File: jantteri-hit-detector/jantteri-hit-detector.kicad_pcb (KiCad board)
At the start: 2 copper layers, 88.9 x 19 mm, 35 parts, among them J1 SWD, J2 main_connector, J3 DBG_PORT, J4 LED_PORT, Q1 Si2319CDS, U1 STM32G030C8T6, U2 AMS1117-3.3, U3 KX023, U4 TXB0104RUT, U5 KX023, U6 KX023, Y1 16MHz

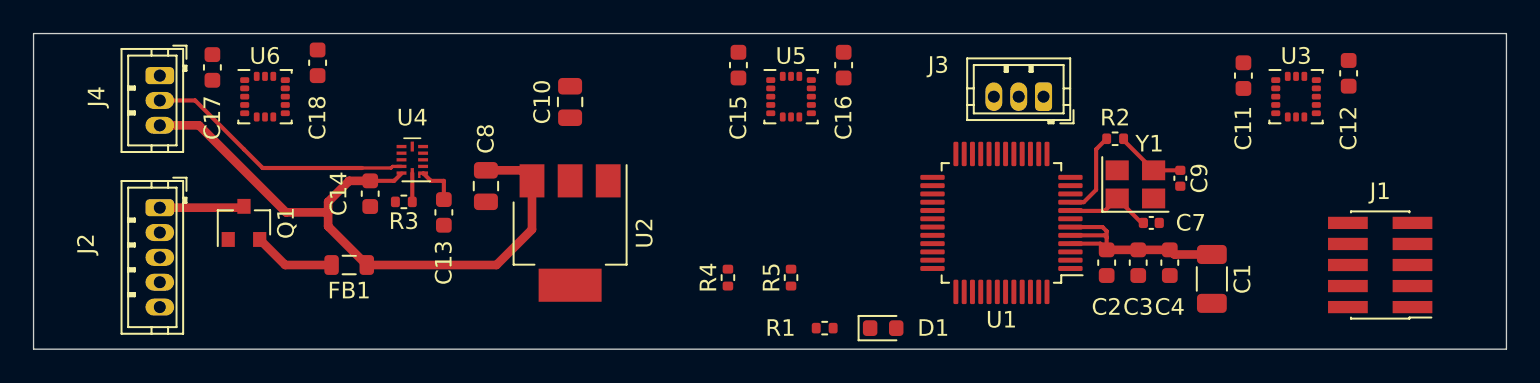
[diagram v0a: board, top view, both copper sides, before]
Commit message: remove hit-detector i2c pullup resistors
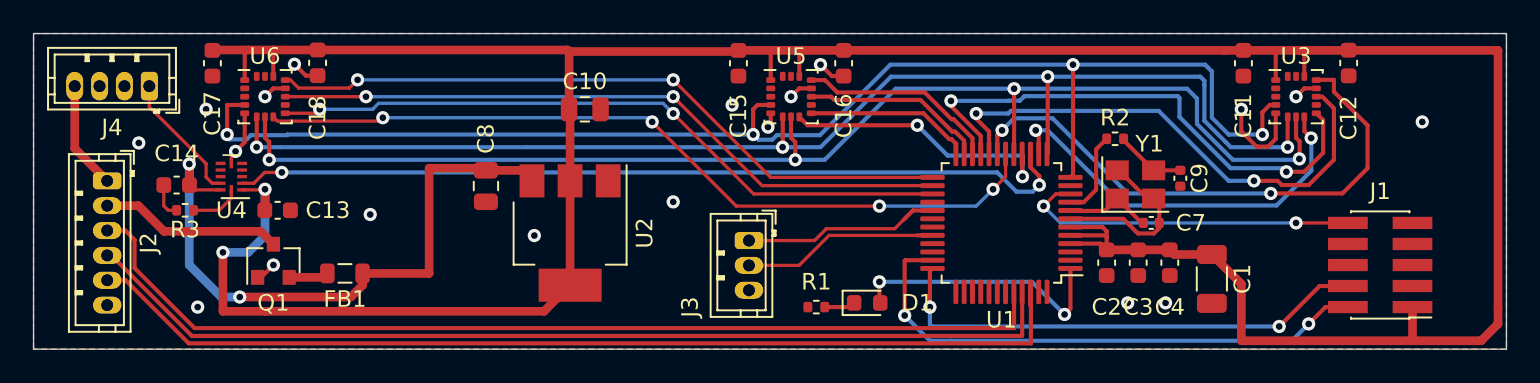
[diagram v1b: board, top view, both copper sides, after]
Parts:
- removed R4, R5: 4K7, Resistor_SMD:R_0402_1005Metric
- J2: value main_connector -> Conn_01x06_Male; footprint Connector_JST2:JST_ZH_B5B-ZR_1x05_P1.50mm_Vertical -> Connector_JST2:JST_ZH_B6B-ZR_1x06_P1.50mm_Vertical
- J4: value LED_PORT -> Conn_01x04_Male; footprint Connector_JST2:JST_ZH_B3B-ZR_1x03_P1.50mm_Vertical -> Connector_JST2:JST_ZH_B4B-ZR_1x04_P1.50mm_Vertical
- moved J3 19.8 mm to (143.5, 112.8), turned to 270 degrees
- moved R3 13.2 mm to (109.5, 111.0)
- moved C14 11.7 mm to (109.0, 109.5), turned to 180 degrees
- moved U4 11.0 mm to (112.3, 109.0)
- moved C13 10.0 mm to (115.1, 111.0), turned to 0 degrees
- moved J2 3.56 mm to (104.8, 109.2)
- moved Q1 2.90 mm to (114.8, 114.0)
- moved D1 1.80 mm to (150.6, 116.6)
- moved R1 1.37 mm to (147.6, 116.8)
- moved C10 0.99 mm to (133.6, 104.9), turned to 0 degrees
- moved J4 0.90 mm to (107.3, 103.5), turned to 180 degrees
- moved C11 0.75 mm to (173.4, 102.1)
- moved C12 0.62 mm to (179.7, 102.1)
- moved FB1 0.57 mm to (119.1, 114.8)
- moved C17 0.25 mm to (111.1, 102.1)
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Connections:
- J2 pad 1: VDC -> +12V
- J2 pad 2: HIT_INT -> VDC
- J2 pad 3: HIT_SCL -> HIT_INT
- J2 pad 4: HIT_SDA -> HIT_SCL
- J2 pad 5: GND -> HIT_SDA
- J4 pad 1: GND -> LED_DATA_5V
- J4 pad 2: LED_DATA_5V -> GND
- J4 pad 3: +5V -> GND
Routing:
- net +3V3: track 17.0 -> 190.8 mm, vias 0 -> 2
- net KX_SCLK: track 0.00 -> 82.9 mm, vias 0 -> 4
- net KX_MISO: track 0.00 -> 78.6 mm, vias 0 -> 4
- net KX_MOSI: track 0.00 -> 77.3 mm, vias 0 -> 4
- net HIT_SDA: track 0.00 -> 60.5 mm
- net HIT_INT: track 0.00 -> 60.4 mm
- net HIT_SCL: track 0.00 -> 59.9 mm
- net LED_DATA_3V3: track 0.00 -> 51.1 mm, vias 0 -> 2
- net KX3_CS: track 0.00 -> 48.7 mm, vias 0 -> 4
- net KX3_INT2: track 0.00 -> 41.9 mm, vias 0 -> 2
- net KX3_TRIG: track 0.00 -> 41.9 mm, vias 0 -> 2
- net KX3_INT1: track 0.00 -> 41.3 mm, vias 0 -> 2
- net KX1_TRIG: track 0.00 -> 33.7 mm, vias 0 -> 2
- net SWDIO: track 0.00 -> 33.2 mm, vias 0 -> 2
- net KX1_INT2: track 0.00 -> 32.1 mm, vias 0 -> 2
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- added copper zone on B.Cu, net GND
- added copper zone on F.Cu, net GND

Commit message: hit-detector update
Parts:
- added C19: 10u, Capacitor_SMD:C_0805_2012Metric, F.Cu at (108.8, 38.3)
- added C20: 100n, Capacitor_SMD:C_0603_1608Metric, F.Cu at (109.6, 50.0)
- added C21: 100n, Capacitor_SMD:C_0603_1608Metric, F.Cu at (101.5, 51.7)
- added C22: 100n, Capacitor_SMD:C_0603_1608Metric, F.Cu at (97.8, 34.4)
- added C23: 100n, Capacitor_SMD:C_0603_1608Metric, F.Cu at (93.3, 34.4)
- added C5: 100n, Capacitor_SMD:C_0603_1608Metric, F.Cu at (133.3, 30.2)
- added C6: 100n, Capacitor_SMD:C_0603_1608Metric, F.Cu at (135.1, 30.2)
- added Q2: IRLML6402TRPBF, Package_TO_SOT_SMD:SOT-23, F.Cu at (112.3, 49.9)
- added R4: 100K, Resistor_SMD:R_0402_1005Metric, F.Cu at (107.2, 48.6)
- added R5: 100K, Resistor_SMD:R_0402_1005Metric, F.Cu at (95.5, 35.1)
- added U7: AP2301, Package_SO:MSOP-8-1EP_3x3mm_P0.65mm_EP1.68x1.88mm, F.Cu at (105.5, 50.9)
- added U8: TXB0104RUT, Package_DFN_QFN:Texas_R_PUQFN-N12, F.Cu at (95.6, 32.0)
- C10: value 10u -> 100n; footprint Capacitor_SMD:C_0805_2012Metric -> Capacitor_SMD:C_0603_1608Metric
- C18: value 100n -> 10u; footprint Capacitor_SMD:C_0603_1608Metric -> Capacitor_SMD:C_0805_2012Metric
- C7: value 12p -> 100n; footprint Capacitor_SMD:C_0402_1005Metric -> Capacitor_SMD:C_0603_1608Metric
- C8: value 10u -> 12p; footprint Capacitor_SMD:C_0805_2012Metric -> Capacitor_SMD:C_0402_1005Metric
- J1: value SWD -> Conn_01x06_Male; footprint Connector_PinHeader_1.27mm:PinHeader_2x05_P1.27mm_Vertical_SMD -> Connector_JST2:JST_ZH_B6B-ZR_1x06_P1.50mm_Vertical; moved to B.Cu
- J2: value Conn_01x06_Male -> SWD; footprint Connector_JST2:JST_ZH_B6B-ZR_1x06_P1.50mm_Vertical -> Connector_PinHeader_1.27mm:PinHeader_2x05_P1.27mm_Horizontal
- J3: value DBG_PORT -> DBG; footprint Connector_JST2:JST_ZH_B3B-ZR_1x03_P1.50mm_Vertical -> Connector_JST2:JST_ZH_B4B-ZR_1x04_P1.50mm_Vertical
- Q1: value Si2319CDS -> IRLML6402TRPBF
- R1: value 1k5 -> 47
- R2: value 47 -> 1k5
- U2: value AMS1117-3.3 -> AP2301; footprint Package_TO_SOT_SMD:SOT-223-3_TabPin2 -> Package_SO:MSOP-8-1EP_3x3mm_P0.65mm_EP1.68x1.88mm
- U4: value TXB0104RUT -> KX023; footprint Package_DFN_QFN:Texas_R_PUQFN-N12 -> Package_LGA:LGA-16_3x3mm_P0.5mm_LayoutBorder3x5y
- U6: value KX023 -> AMS1117-3.3; footprint Package_LGA:LGA-16_3x3mm_P0.5mm_LayoutBorder3x5y -> Package_TO_SOT_SMD:SOT-223-3_TabPin2
- moved J1 143.7 mm to (62.5, 33.9), turned to 270 degrees
- moved C12 120.7 mm to (85.0, 27.3), turned to 90 degrees
- moved U3 117.8 mm to (83.9, 31.2)
- moved C9 93.0 mm to (122.2, 29.1), turned to 90 degrees
- moved C4 91.9 mm to (131.6, 30.2), turned to 90 degrees
- moved C3 91.8 mm to (129.8, 30.2), turned to 90 degrees
- moved C2 91.7 mm to (128.1, 30.2), turned to 90 degrees
- moved C1 90.8 mm to (139.1, 30.4), turned to 90 degrees
- moved Y1 90.6 mm to (125.0, 29.1), turned to 180 degrees
- moved C11 90.0 mm to (99.6, 50.5)
- moved C13 89.6 mm to (83.1, 27.3), turned to 90 degrees
- moved R1 88.5 mm to (123.7, 31.6), turned to 180 degrees
- moved C7 87.2 mm to (136.9, 30.2), turned to 90 degrees
- moved D1 85.5 mm to (133.1, 32.9), turned to 180 degrees
- moved C8 82.8 mm to (125.1, 26.8), turned to 180 degrees
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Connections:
- net DBG_RX renamed /jst-dbg/DBG_RX
- net DBG_TX renamed /jst-dbg/DBG_TX
- net STATUS_LED renamed Net-(D1-Pad2)
- C10 pad 1: +3V3 -> Net-(C10-Pad1)
- C11 pad 1: +3V3 -> /power_protect/OUT
- C14 pad 1: +5V -> +3V3
- C18 pad 1: +3V3 -> +5V
- C7 pad 1: HSE_IN -> +3V3
- C8 pad 1: +5V -> /STM32G030C8T6/HSE_IN
- FB1 pad 2: Net-(FB1-Pad2) -> /power_protect/OUT
- J1 pad 1: +3V3 -> +12V
- J1 pad 2: SWDIO -> VCC
- J1 pad 3: GND -> HIT_INT
- J1 pad 4: SWCLK -> HIT_SCL
- J1 pad 5: GND -> HIT_SDA
- J1 pad 6: (no net) -> GND
- J2 pad 1: +12V -> +3V3
- J2 pad 2: VDC -> /10pinARM/SWDIO
- J2 pad 3: HIT_INT -> GND
- J2 pad 4: HIT_SCL -> /10pinARM/SWCLK
- J2 pad 5: HIT_SDA -> GND
- J2 pad 6: GND -> /10pinARM/SWO
- J3 pad 3: GND -> USB-5V
- J4 pad 1: LED_DATA_5V -> Net-(J4-Pad1)
- Q1 pad 2: Net-(FB1-Pad2) -> Net-(C10-Pad1)
- Q1 pad 3: VDC -> VCC
- R1 pad 1: GND -> /STM32G030C8T6/HSE_OUT
- R1 pad 2: Net-(D1-Pad1) -> Net-(C9-Pad1)
- R2 pad 1: HSE_OUT -> GND
- R2 pad 2: Net-(C9-Pad1) -> Net-(D1-Pad1)
- R3 pad 1: Net-(R3-Pad1) -> /power_protect/EN
- U1 pad 10: NRST -> /10pinARM/NRST
- U1 pad 11: (no net) -> /STM32G030C8T6/PA0
- U1 pad 14: KX1_CS -> /STM32G030C8T6/PA3
- U1 pad 16: KX2_CS -> /STM32G030C8T6/PA5
- U1 pad 18: KX3_CS -> /STM32G030C8T6/PA7
- U1 pad 19: KX1_TRIG -> KX1_INT1
- U1 pad 2: (no net) -> Net-(U1-Pad2)
- U1 pad 20: KX1_INT1 -> KX1_INT2
- U1 pad 21: KX1_INT2 -> KX2_TRIG
- U1 pad 22: KX2_TRIG -> KX1_CS
- U1 pad 23: KX2_INT1 -> KX2_INT2
- U1 pad 24: KX2_INT2 -> KX2_CS
- U1 pad 26: KX3_INT1 -> KX3_CS
- U1 pad 27: KX3_INT2 -> /STM32G030C8T6/PB15
- U1 pad 28: (no net) -> /STM32G030C8T6/PA8
- U1 pad 3: (no net) -> Net-(U1-Pad3)
- U1 pad 30: (no net) -> /STM32G030C8T6/PC6
- U1 pad 31: (no net) -> /STM32G030C8T6/PC7
- U1 pad 33: (no net) -> /STM32G030C8T6/PA11
- U1 pad 34: (no net) -> /STM32G030C8T6/PA12
- U1 pad 35: SWDIO -> /10pinARM/SWDIO
- U1 pad 36: SWCLK -> /10pinARM/SWCLK
- U1 pad 37: (no net) -> /STM32G030C8T6/PA15
- U1 pad 38: (no net) -> /STM32G030C8T6/PD0
- U1 pad 39: (no net) -> /STM32G030C8T6/PD1
- U1 pad 40: (no net) -> /STM32G030C8T6/PD2
- U1 pad 41: (no net) -> /STM32G030C8T6/PD3
- U1 pad 42: (no net) -> KX2_INT1
- U1 pad 43: (no net) -> KX3_INT1
- U1 pad 44: HIT_INT -> KX3_INT2
- U1 pad 47: (no net) -> HIT_INT
- U1 pad 48: (no net) -> KX1_TRIG
- U1 pad 8: HSE_IN -> /STM32G030C8T6/HSE_IN
- U1 pad 9: HSE_OUT -> /STM32G030C8T6/HSE_OUT
- U2 pad 2: +3V3 -> Net-(C10-Pad1)
- U2 pad 3: +5V -> Net-(C10-Pad1)
- U4 pad 10: LED_DATA_5V -> (no net)
- U4 pad 11: +5V -> KX2_INT1
- U4 pad 12: Net-(R3-Pad1) -> GND
- U4 pad 2: LED_DATA_3V3 -> (no net)
- U4 pad 4: (no net) -> KX_SCLK
- U4 pad 5: (no net) -> GND
- U4 pad 6: GND -> KX_MOSI
- U4 pad 7: (no net) -> KX_MISO
- U4 pad 8: (no net) -> KX2_CS
- U4 pad 9: (no net) -> KX2_INT2
- U5 pad 11: KX2_INT1 -> KX3_INT1
- U5 pad 13: KX2_TRIG -> KX3_TRIG
- U5 pad 8: KX2_CS -> KX3_CS
- U5 pad 9: KX2_INT2 -> KX3_INT2
- U6 pad 1: +3V3 -> GND
- U6 pad 2: (no net) -> +3V3
- U6 pad 3: (no net) -> +5V
- Y1 pad 1: HSE_IN -> /STM32G030C8T6/HSE_IN
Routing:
- net VCC: track 0.00 -> 57.6 mm, vias 0 -> 2
- net +3V3: track 190.8 -> 144.2 mm
- net SWDIO: track 33.2 -> 0.00 mm, vias 2 -> 0
- net SWCLK: track 29.7 -> 0.00 mm, vias 2 -> 0
- net /10pinARM/NRST: track 0.00 -> 24.9 mm, vias 0 -> 2
- net /10pinARM/SWDIO: track 0.00 -> 21.8 mm
- net KX3_INT2: track 41.9 -> 20.5 mm
- net NRST: track 20.7 -> 0.00 mm, vias 2 -> 0
- net KX1_CS: track 24.3 -> 43.7 mm
- net /10pinARM/SWCLK: track 0.00 -> 19.3 mm
- net KX2_INT1: track 11.1 -> 30.2 mm, vias 0 -> 2
- net LED_DATA_3V3: track 51.1 -> 32.2 mm, vias 2 -> 4
- net USB-5V: track 0.00 -> 18.1 mm
- net Net-(J4-Pad1): track 0.00 -> 17.9 mm
- net KX3_INT1: track 41.3 -> 23.5 mm
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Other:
- board size 88.9 x 19 mm -> 103.9 x 29.1 mm

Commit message: jantteri-pwr-motor
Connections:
- J3 pad 4: /jst-dbg/GND -> GND

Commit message: random changes
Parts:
- U3, U4, U5: value KX023 -> LIS2DW12TR; footprint Package_LGA:LGA-16_3x3mm_P0.5mm_LayoutBorder3x5y -> Package_LGA:LGA-12_2x2mm_P0.5mm
- moved C13 7.78 mm to (90.3, 30.1), turned to 270 degrees
- moved C14 6.73 mm to (106.9, 30.1), turned to 270 degrees
- moved C15 6.05 mm to (109.7, 30.1), turned to 270 degrees
- moved C12 3.63 mm to (87.2, 30.1), turned to 270 degrees
- moved C16 2.81 mm to (145.7, 28.7), turned to 0 degrees
- moved C17 0.86 mm to (145.7, 27.1), turned to 0 degrees
- moved U3 0.18 mm to (83.8, 31.1), turned to 90 degrees
- moved U4 0.14 mm to (114.0, 31.1), turned to 90 degrees
- moved U5 0.13 mm to (144.1, 31.1), turned to 90 degrees
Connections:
- U1 pad 21: KX2_TRIG -> KX2_INT1
- U1 pad 25: KX3_TRIG -> /STM32G030C8T6/PB13
- U1 pad 42: KX2_INT1 -> /STM32G030C8T6/PB3
- U1 pad 48: KX1_TRIG -> /STM32G030C8T6/PB9
- U3 pad 1: +3V3 -> KX_SCLK
- U3 pad 10: (no net) -> +3V3
- U3 pad 11: KX1_INT1 -> KX1_INT2
- U3 pad 12: GND -> KX1_INT1
- U3 pad 2: (no net) -> KX1_CS
- U3 pad 3: (no net) -> KX_MISO
- U3 pad 4: KX_SCLK -> KX_MOSI
- U3 pad 6: KX_MOSI -> GND
- U3 pad 7: KX_MISO -> GND
- U3 pad 8: KX1_CS -> GND
- U3 pad 9: KX1_INT2 -> +3V3
- U4 pad 1: +3V3 -> KX_SCLK
- U4 pad 10: (no net) -> +3V3
- U4 pad 11: KX2_INT1 -> KX2_INT2
- U4 pad 12: GND -> KX2_INT1
- U4 pad 2: (no net) -> KX2_CS
- U4 pad 3: (no net) -> KX_MISO
- U4 pad 4: KX_SCLK -> KX_MOSI
- U4 pad 6: KX_MOSI -> GND
- U4 pad 7: KX_MISO -> GND
- U4 pad 8: KX2_CS -> GND
- U4 pad 9: KX2_INT2 -> +3V3
- U5 pad 1: +3V3 -> KX_SCLK
- U5 pad 10: (no net) -> +3V3
- U5 pad 11: KX3_INT1 -> KX3_INT2
- U5 pad 12: GND -> KX3_INT1
- U5 pad 2: (no net) -> KX3_CS
- U5 pad 3: (no net) -> KX_MISO
- U5 pad 4: KX_SCLK -> KX_MOSI
- U5 pad 6: KX_MOSI -> GND
- U5 pad 7: KX_MISO -> GND
- U5 pad 8: KX3_CS -> GND
- U5 pad 9: KX3_INT2 -> +3V3
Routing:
- net KX1_TRIG: track 50.7 -> 0.00 mm, vias 4 -> 0
- net KX3_TRIG: track 40.0 -> 0.00 mm, vias 2 -> 0
- net KX2_TRIG: track 14.5 -> 0.00 mm
- net KX2_INT1: track 30.2 -> 18.0 mm
- net KX2_INT2: track 13.4 -> 23.8 mm, vias 0 -> 2
- net GND: track 47.9 -> 41.4 mm
- net KX1_INT2: track 42.4 -> 48.4 mm, vias 2 -> 3
- net KX_MOSI: track 68.6 -> 74.1 mm
- net KX3_INT1: track 23.5 -> 19.3 mm
- net KX_SCLK: track 68.5 -> 65.0 mm
- net KX_MISO: track 69.0 -> 72.4 mm
- net KX1_INT1: track 42.9 -> 46.2 mm, vias 2 -> 3
- net +3V3: track 144.2 -> 147.4 mm
- net KX2_CS: track 14.0 -> 16.8 mm
- net KX1_CS: track 43.7 -> 45.5 mm
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
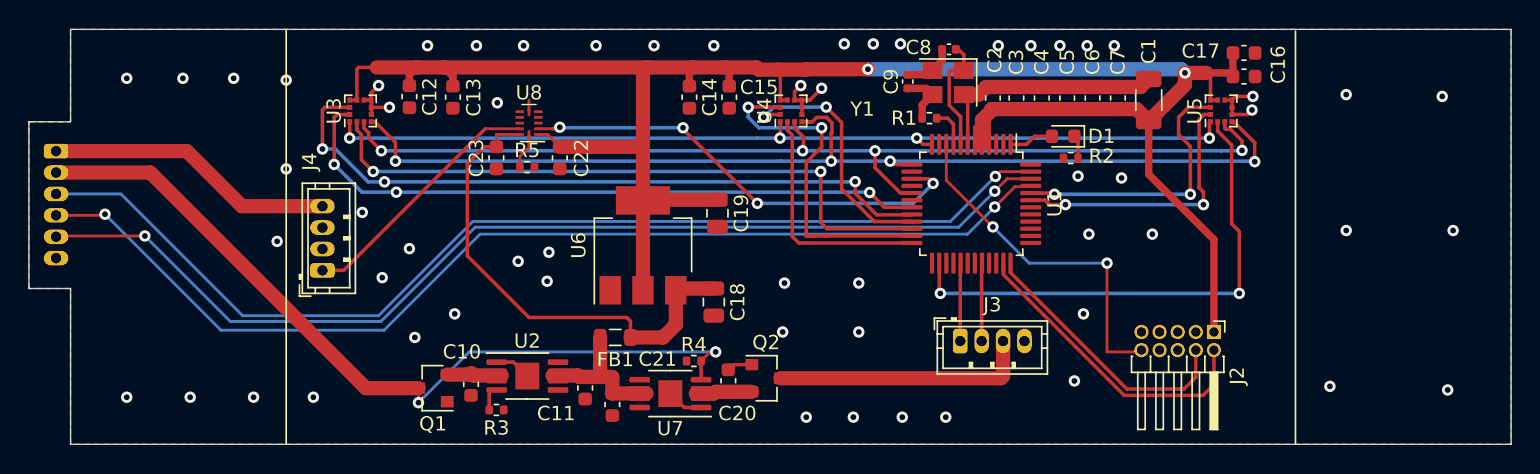
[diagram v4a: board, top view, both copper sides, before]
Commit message: Tuubijantteri design Ordered
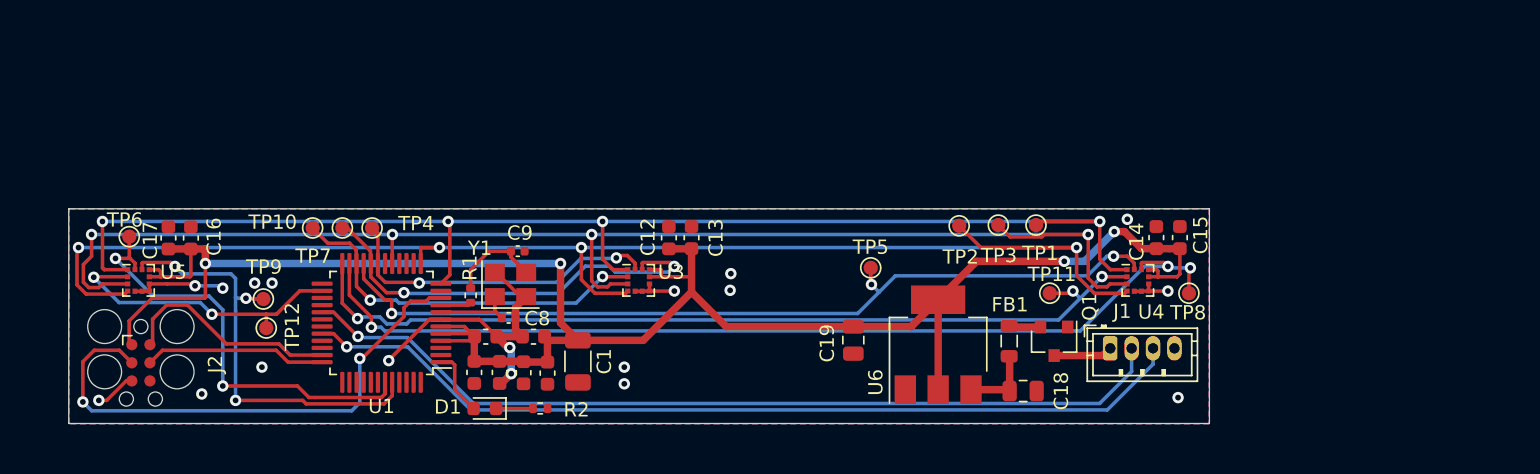
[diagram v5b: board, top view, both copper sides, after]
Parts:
- removed C10, C11, C20, C21, C22, C23: 100n, Capacitor_SMD:C_0603_1608Metric
- removed J3: DBG, Connector_JST2:JST_ZH_B4B-ZR_1x04_P1.50mm_Vertical
- removed J4: Conn_01x04_Male, Connector_JST2:JST_ZH_B4B-ZR_1x04_P1.50mm_Vertical
- removed Q2: IRLML6402TRPBF, Package_TO_SOT_SMD:SOT-23
- removed R3, R4, R5: 100K, Resistor_SMD:R_0402_1005Metric
- removed U2, U7: AP2301, Package_SO:MSOP-8-1EP_3x3mm_P0.65mm_EP1.68x1.88mm
- removed U8: TXB0104RUT, Package_DFN_QFN:Texas_R_PUQFN-N12
- added TP1: TestPoint, TestPoint:TestPoint_Pad_D1.0mm, F.Cu at (131.2, 39.1)
- added TP10: TestPoint, TestPoint:TestPoint_Pad_D1.0mm, F.Cu at (80.5, 39.3)
- added TP11: TestPoint, TestPoint:TestPoint_Pad_D1.0mm, F.Cu at (132.1, 43.9)
- added TP12: TestPoint, TestPoint:TestPoint_Pad_D1.0mm, F.Cu at (77.2, 46.3)
- added TP2: TestPoint, TestPoint:TestPoint_Pad_D1.0mm, F.Cu at (125.8, 39.2)
- added TP3: TestPoint, TestPoint:TestPoint_Pad_D1.0mm, F.Cu at (128.5, 39.1)
- added TP4: TestPoint, TestPoint:TestPoint_Pad_D1.0mm, F.Cu at (84.6, 39.3)
- added TP5: TestPoint, TestPoint:TestPoint_Pad_D1.0mm, F.Cu at (119.6, 42.1)
- added TP6: TestPoint, TestPoint:TestPoint_Pad_D1.0mm, F.Cu at (67.6, 39.9)
- added TP7: TestPoint, TestPoint:TestPoint_Pad_D1.0mm, F.Cu at (82.5, 39.3)
- added TP8: TestPoint, TestPoint:TestPoint_Pad_D1.0mm, F.Cu at (141.9, 43.9)
- added TP9: TestPoint, TestPoint:TestPoint_Pad_D1.0mm, F.Cu at (77.0, 44.3)
- J1: value Conn_01x06_Male -> Conn_01x04_Male; footprint Connector_JST2:JST_ZH_B6B-ZR_1x06_P1.50mm_Vertical -> Connector_JST2:JST_ZH_B4B-ZR_1x04_P1.50mm_Vertical; moved to F.Cu
- J2: value SWD -> Conn_02x03_Odd_Even; footprint Connector_PinHeader_1.27mm:PinHeader_2x05_P1.27mm_Horizontal -> Connector:Tag-Connect_TC2030-IDC-FP_2x03_P1.27mm_Vertical
- moved U5 76.8 mm to (68.3, 43.0), turned to 0 degrees
- moved C17 76.5 mm to (70.4, 40.0), turned to 90 degrees
- moved J2 75.2 mm to (68.4, 48.8)
- moved J1 75.2 mm to (136.4, 47.8), turned to 0 degrees
- moved C16 74.7 mm to (71.9, 40.0), turned to 90 degrees
- moved C7 49.0 mm to (91.8, 49.4), turned to 270 degrees
- moved C6 45.8 mm to (93.6, 49.4), turned to 270 degrees
- moved D1 44.8 mm to (92.5, 52.0)
- moved C1 44.0 mm to (99.1, 48.7), turned to 270 degrees
- moved Q1 43.7 mm to (132.4, 47.3), turned to 270 degrees
- moved U1 42.2 mm to (85.3, 46.0), turned to 180 degrees
- moved C5 41.2 mm to (96.9, 49.5), turned to 270 degrees
- moved R2 41.1 mm to (96.4, 52.0), turned to 180 degrees
- moved C4 41.1 mm to (95.2, 49.5), turned to 270 degrees
- moved C2 39.3 mm to (92.6, 46.9), turned to 0 degrees
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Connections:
- net +5V renamed /AMS1117-3.3/VIN
- net /10pinARM/SWCLK renamed /STM32G030C8T6/SWCLK
- net /10pinARM/SWDIO renamed /STM32G030C8T6/SWDIO
- net /10pinARM/SWO renamed /TC2030/SWO
- FB1 pad 2: /power_protect/OUT -> Net-(FB1-Pad2)
- J1 pad 1: +12V -> VCC
- J1 pad 2: VCC -> HIT_TX
- J1 pad 3: HIT_INT -> HIT_RX
- J1 pad 4: HIT_SCL -> GND
- J2 pad 3: GND -> /STM32G030C8T6/NRST
- Q1 pad 2: Net-(C10-Pad1) -> Net-(FB1-Pad2)
- U1 pad 10: /10pinARM/NRST -> /STM32G030C8T6/NRST
- U1 pad 15: LED_DATA_3V3 -> /STM32G030C8T6/PA4
- U1 pad 29: /jst-dbg/DBG_TX -> HIT_TX
- U1 pad 32: /jst-dbg/DBG_RX -> HIT_RX
- U1 pad 45: HIT_SCL -> /STM32G030C8T6/PB6
- U1 pad 46: HIT_SDA -> /STM32G030C8T6/PB7
- U1 pad 47: HIT_INT -> /STM32G030C8T6/PB8
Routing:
- net HIT_INT: track 76.0 -> 0.00 mm, vias 1 -> 0
- net HIT_SCL: track 75.9 -> 0.00 mm, vias 2 -> 0
- net HIT_SDA: track 75.0 -> 0.00 mm, vias 2 -> 0
- net HIT_RX: track 0.00 -> 62.9 mm, vias 0 -> 1
- net HIT_TX: track 0.00 -> 61.9 mm, vias 0 -> 1
- net VCC: track 57.6 -> 4.14 mm, vias 2 -> 0
- net KX2_CS: track 16.8 -> 62.3 mm, vias 0 -> 3
- net KX2_INT2: track 23.8 -> 68.8 mm, vias 2 -> 3
- net KX2_INT1: track 18.0 -> 60.8 mm, vias 2 -> 3
- net /STM32G030C8T6/NRST: track 0.00 -> 37.7 mm, vias 0 -> 2
- net LED_DATA_3V3: track 32.2 -> 0.00 mm, vias 4 -> 0
- net /AMS1117-3.3/VIN: track 34.6 -> 5.20 mm
- net KX_SCLK: track 65.0 -> 93.8 mm
- net KX_MOSI: track 74.1 -> 99.8 mm
- net KX_MISO: track 72.4 -> 97.7 mm
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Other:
- board size 103.9 x 29.1 mm -> 79.9 x 15 mm
- rule trace_min: 0.2 -> 0.127

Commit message: Update projects
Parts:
- moved J1 30.6 mm to (105.7, 48.8)
- moved C19 3.06 mm to (116.1, 45.1), turned to 90 degrees
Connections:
- J1 pad 1: VCC -> HIT_TX
- J1 pad 2: HIT_TX -> HIT_RX
- J1 pad 3: HIT_RX -> VCC
- U1 pad 2: Net-(U1-Pad2) -> unconnected-(U1-PC14-OSC32_IN-Pad2)
- U1 pad 3: Net-(U1-Pad3) -> unconnected-(U1-PC15-OSC32_OUT-Pad3)
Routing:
- net HIT_TX: track 61.9 -> 28.4 mm
- net HIT_RX: track 62.9 -> 29.9 mm
- net VCC: track 4.14 -> 30.2 mm, vias 0 -> 1
- net GND: track 37.3 -> 34.8 mm
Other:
- net class Default removed
